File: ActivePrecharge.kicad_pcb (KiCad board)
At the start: 2 copper layers, 93.5 x 61.5 mm, 64 parts, among them IC1 AMC1311BDWVR, IC2 AMC1311BDWVR, IC3 1769205241, J1 Conn_01x02, J2 Conn_01x03, J3 Conn_01x02, Q1 IRLML0030, Q2 PMV35EPER, U3 AP63203WU, U4 Nucleo_L432KC

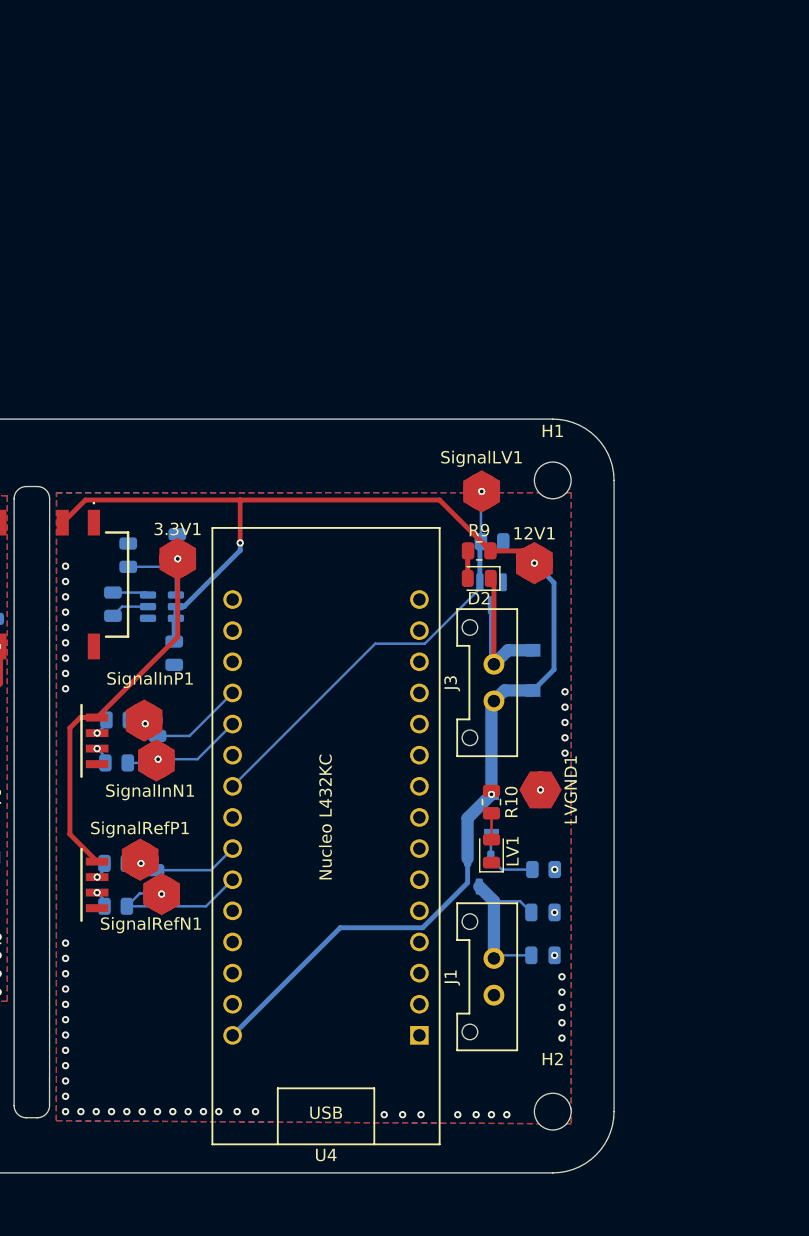
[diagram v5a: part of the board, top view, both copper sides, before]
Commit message: added contactor signal connectors from v.3
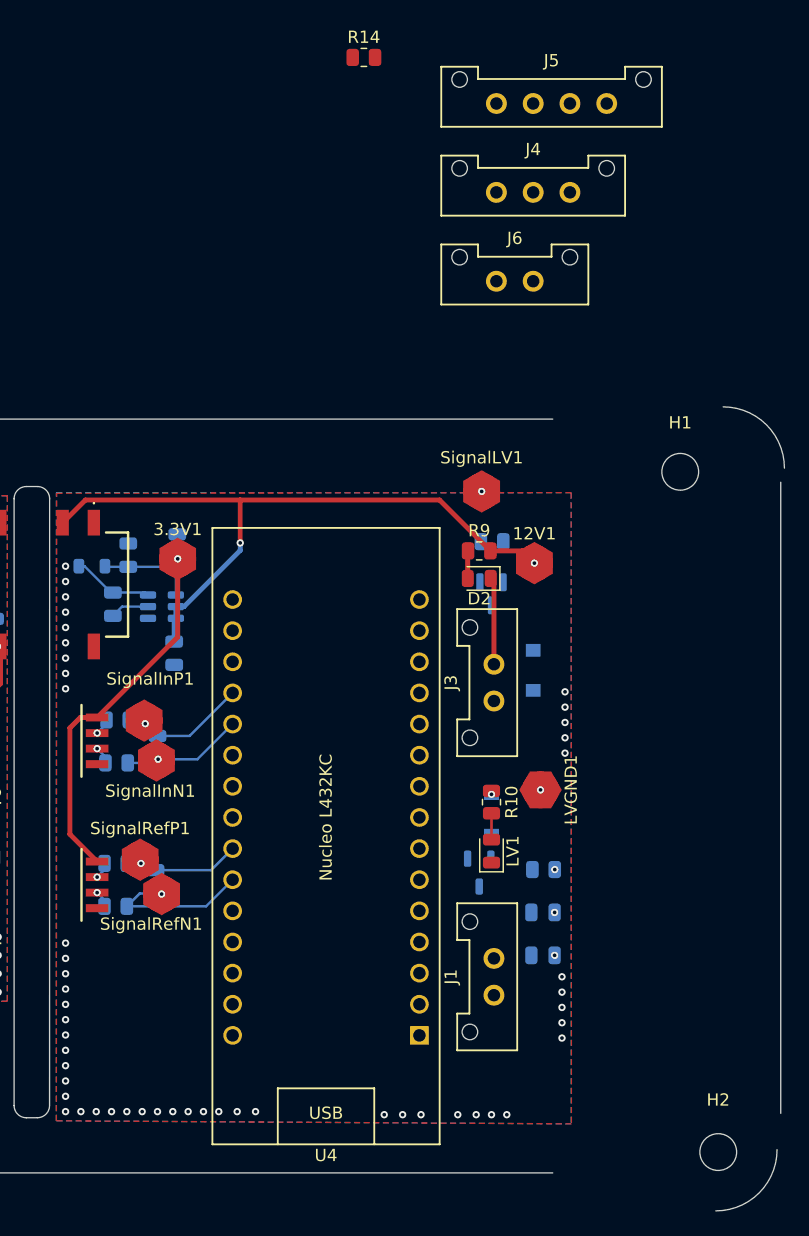
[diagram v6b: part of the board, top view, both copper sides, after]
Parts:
- added J4: Conn_01x03, utsvt-conn:Molex_MicroFit3.0_1x3xP3.00mm_PolarizingPeg_Vertical, F.Cu at (157.9, 41.0)
- added J5: Conn_01x04, utsvt-conn:Molex_MicroFit3.0_1x4xP3.00mm_PolarizingPeg_Vertical, F.Cu at (157.9, 33.8)
- added J6: Conn_01x02, utsvt-conn:Molex_MicroFit3.0_1x2xP3.00mm_PolarizingPeg_Vertical, F.Cu at (157.9, 48.2)
- added L1: 10u, Inductor_SMD:L_0805_2012Metric, B.Cu at (124.9, 71.5)
- added R14: R_US, Resistor_SMD:R_0805_2012Metric, F.Cu at (147.1, 30.0)
- moved H2 13.9 mm to (176.0, 119.3)
- moved H1 10.4 mm to (172.9, 63.8)
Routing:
- net /LV+: track 111.1 -> 55.5 mm
- net /SignalLV: track 34.8 -> 0.00 mm
- net +12V: track 12.9 -> 0.00 mm
- net Net-(D1-A): track 15.7 -> 7.11 mm
- net Net-(D7-A): track 5.75 -> 0.00 mm
- net Net-(U3-BST): track 2.95 -> 6.61 mm
- net /3.3V: track 37.4 -> 39.3 mm
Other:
- board size 93.5 x 61.5 mm -> 107.4 x 65.6 mm

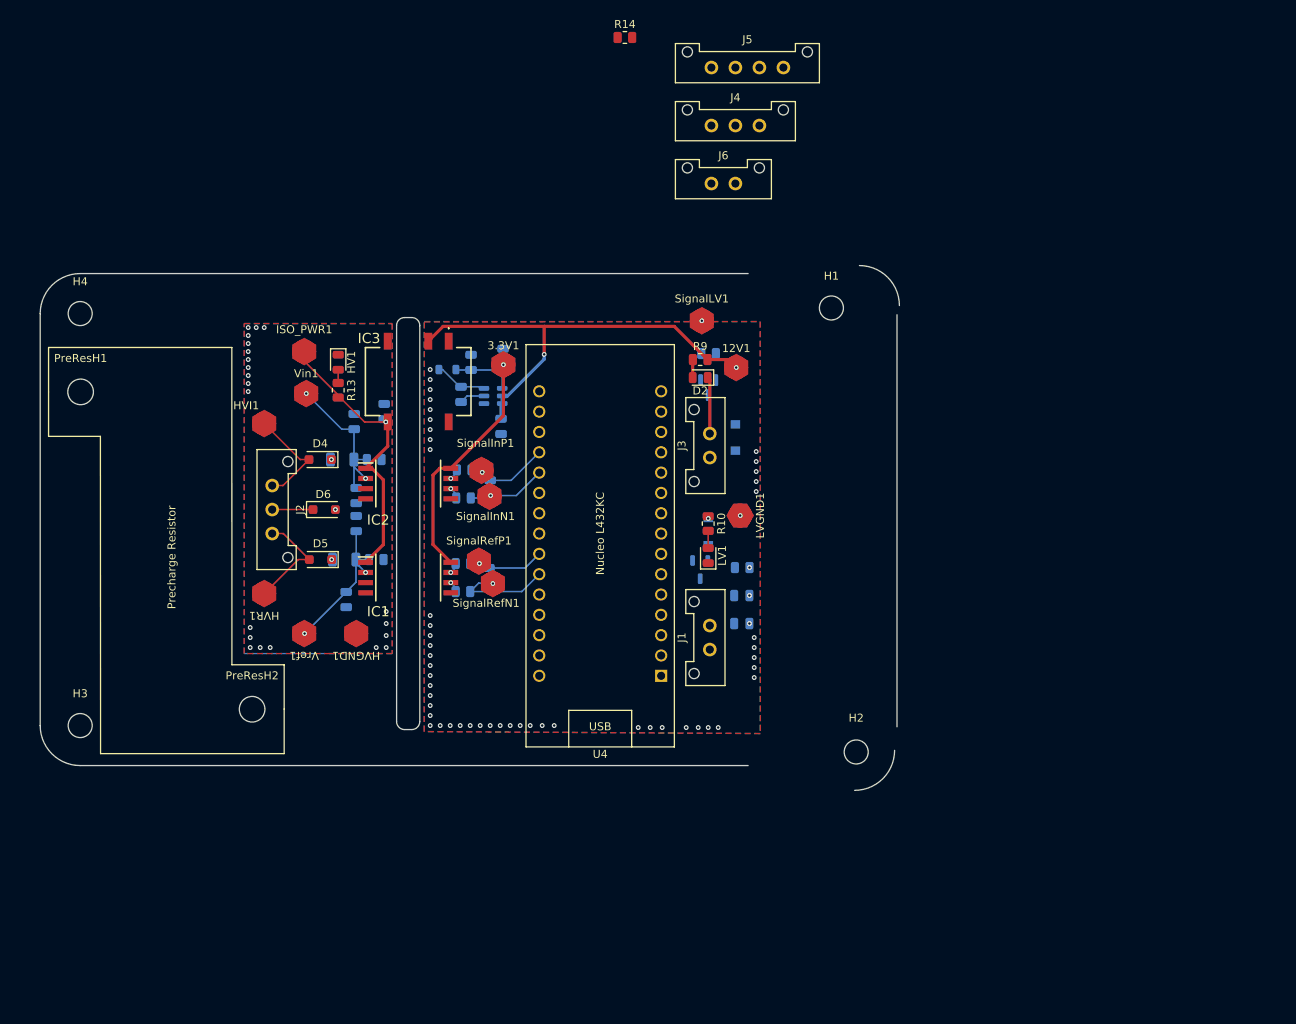
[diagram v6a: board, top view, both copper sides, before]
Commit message: verify controls signals and reverse polarity schematics
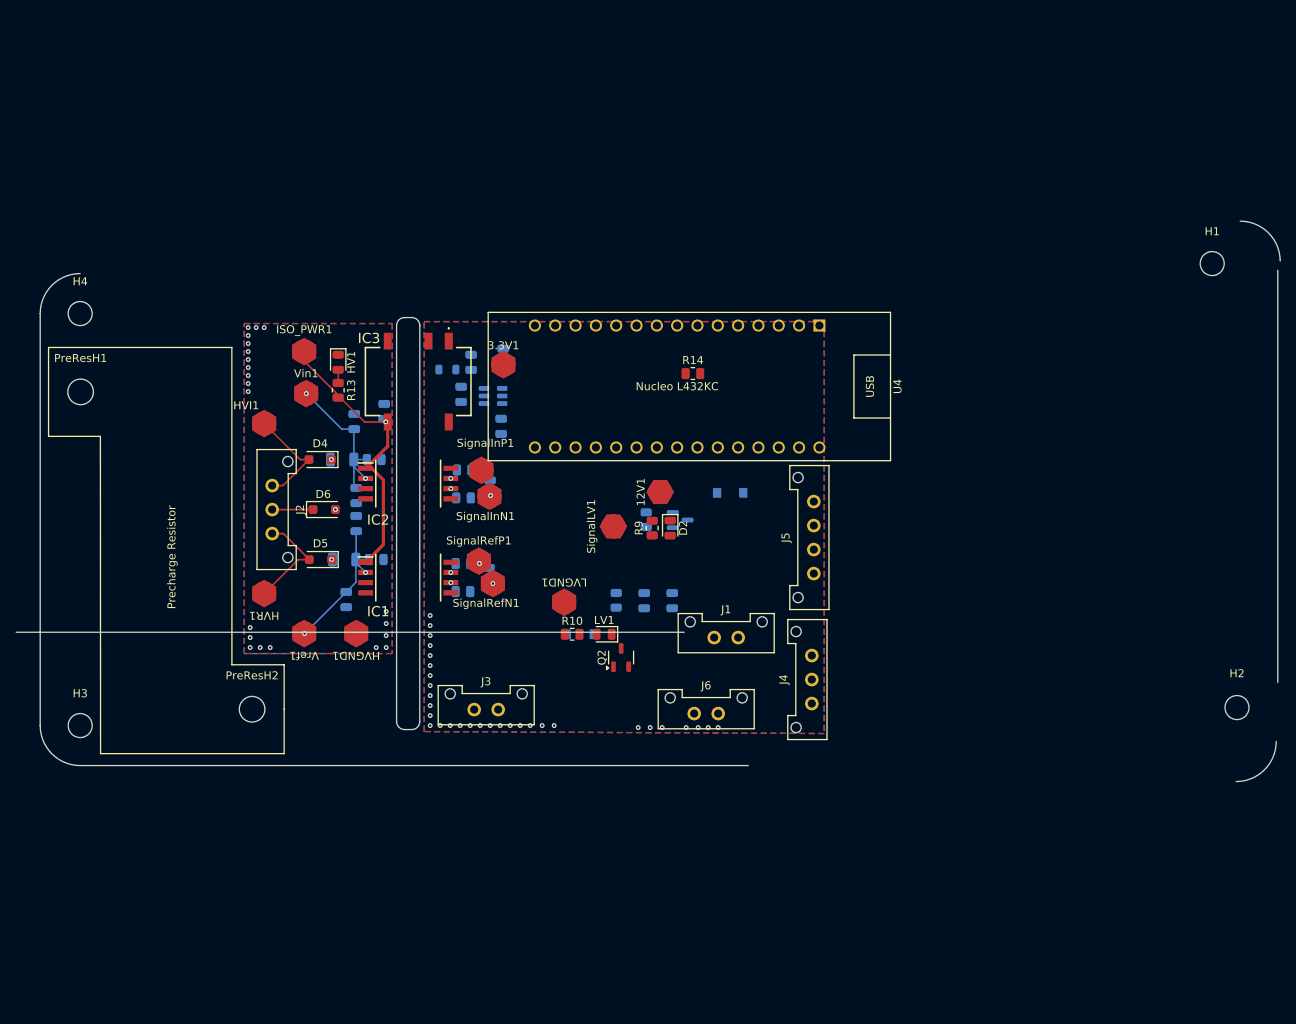
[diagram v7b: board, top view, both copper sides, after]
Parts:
- Q2: moved to F.Cu
- moved J4 73.3 mm to (170.4, 113.2), turned to 90 degrees
- moved J6 66.3 mm to (155.8, 114.5)
- moved J5 64.5 mm to (170.7, 97.0), turned to 90 degrees
- moved H1 47.9 mm to (220.5, 58.2)
- moved H2 47.9 mm to (223.6, 113.8)
- moved J3 43.1 mm to (128.2, 114.0), turned to 0 degrees
- moved R14 42.9 mm to (155.6, 72.0)
- moved SignalLV1 28.0 mm to (145.7, 91.1), turned to 90 degrees
- moved LVGND1 24.5 mm to (139.5, 100.6), turned to 180 degrees
- moved R11 22.2 mm to (149.8, 90.3), turned to 90 degrees
- moved R10 21.9 mm to (140.5, 104.6), turned to 0 degrees
- moved R9 21.9 mm to (150.5, 91.3), turned to 90 degrees
- moved U4 20.7 mm to (153.6, 73.6), turned to 180 degrees
- moved D7 20.5 mm to (141.5, 104.6), turned to 0 degrees
- moved D2 19.2 mm to (152.8, 91.3), turned to -90 degrees
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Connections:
- Q2 pad 1: /LV+ -> Net-(D7-A)
- Q2 pad 2: Net-(D7-A) -> /LV+
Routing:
- net /LV+: track 55.5 -> 0.00 mm, vias 3 -> 0
- net /3.3V: track 39.3 -> 0.00 mm, vias 1 -> 0
- net /SignalRefN: track 12.3 -> 0.00 mm
- net /SignalInP: track 10.5 -> 0.00 mm, vias 1 -> 0
- net /SignalInN: track 9.87 -> 0.00 mm
- net /SignalRefP: track 9.59 -> 0.00 mm
- net Net-(D1-A): track 7.11 -> 0.00 mm
- net Net-(U3-BST): track 6.61 -> 0.00 mm
- net Net-(U3-SW): track 3.17 -> 0.00 mm
- net Net-(D2-A): track 2.26 -> 0.00 mm
- net Net-(LV1-A): track 2.15 -> 0.00 mm
- net Net-(IC2-VOUTN): track 1.44 -> 0.00 mm
- net Net-(IC2-VOUTP): track 1.38 -> 0.00 mm
- net Net-(IC1-VOUTP): track 1.36 -> 0.00 mm
- net Net-(IC1-VOUTN): track 1.36 -> 0.00 mm
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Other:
- board size 107.4 x 65.6 mm -> 158 x 70 mm

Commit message: layout update with controls signals and fuses
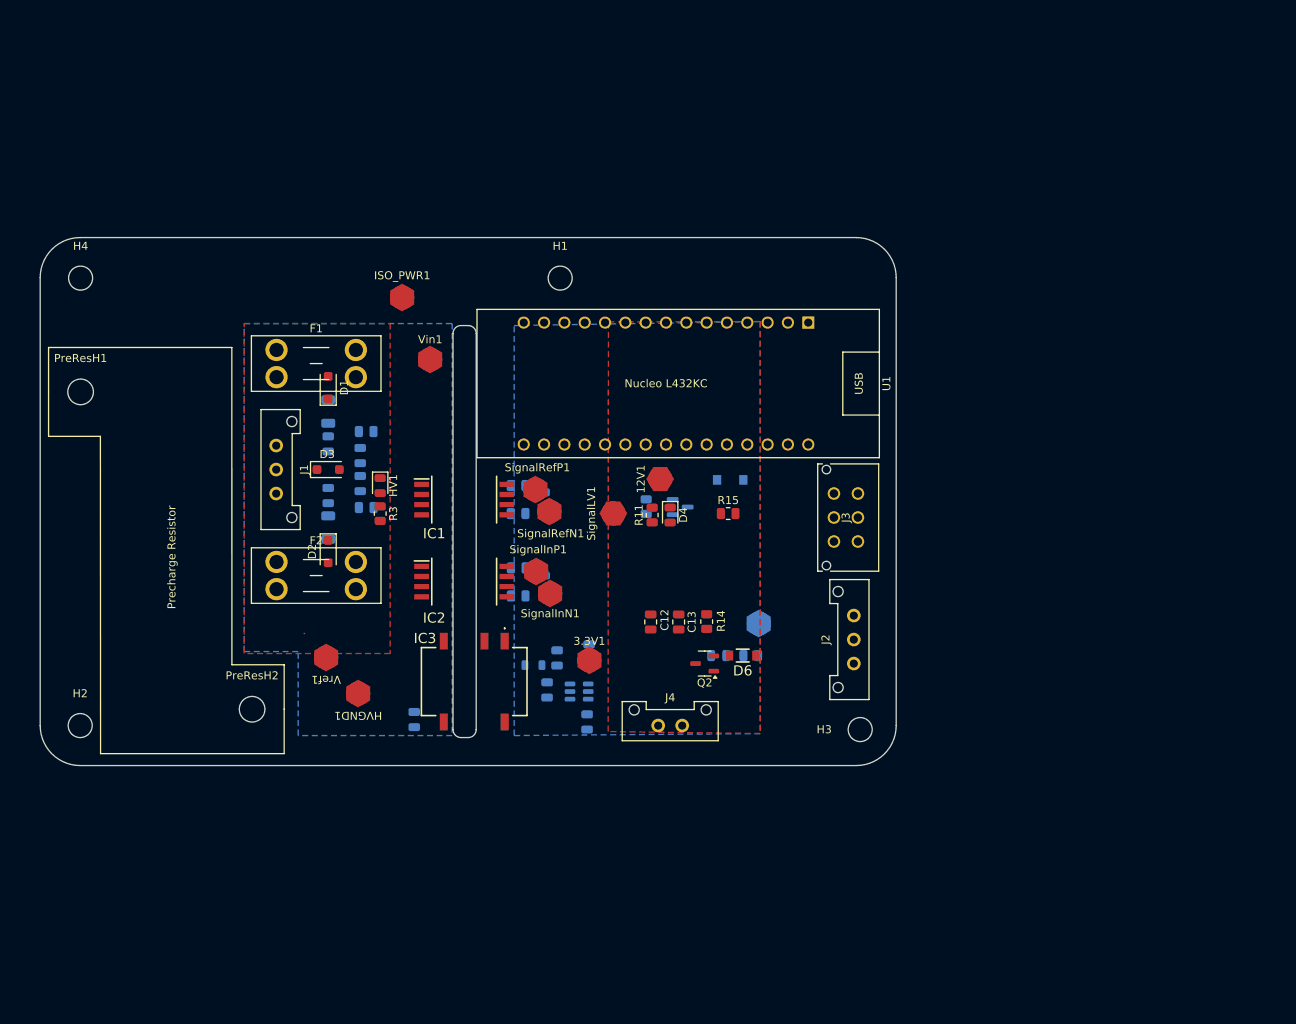
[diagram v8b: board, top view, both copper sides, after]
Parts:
- removed HVI1, HVR1: TestPoint, Active-PrechargeLib:TestPoint_HEX_3mmID
- removed the J4 at (170.4, 113.2)
- removed J5: Conn_01x04, utsvt-conn:Molex_MicroFit3.0_1x4xP3.00mm_PolarizingPeg_Vertical
- removed J6: Conn_01x02, utsvt-conn:Molex_MicroFit3.0_1x2xP3.00mm_PolarizingPeg_Vertical
- removed the R14 at (155.6, 72.0)
- added F1: Fuse, Fuse:Fuseholder_Blade_Mini_Keystone_3568, F.Cu at (103.5, 69.0)
- added F2: Fuse, Fuse:Fuseholder_Blade_Mini_Keystone_3568, F.Cu at (103.5, 95.5)
- added J2: Conn_01x03, utsvt-conn:Molex_MicroFit3.0_1x3xP3.00mm_PolarizingPeg_Vertical, F.Cu at (175.7, 108.2)
- added R15: 10k, Resistor_SMD:R_0805_2012Metric, F.Cu at (160.0, 89.5)
- C12: renamed from C1; moved to F.Cu
- C13: renamed from C2; moved to F.Cu
- D6: renamed from D7; moved to F.Cu
- J3: value Conn_01x02 -> Conn_02x03_Top_Bottom; footprint utsvt-conn:Molex_MicroFit3.0_1x2xP3.00mm_PolarizingPeg_Vertical -> Active-PrechargeLib:CONN_SD-43045-005_06_MOL
- LV1, LVGND1: moved to B.Cu
- R13: renamed from R10; moved to B.Cu
- R14: renamed from R12; moved to F.Cu
- moved H1 81.5 mm to (139.0, 60.1)
- moved J3 55.0 mm to (176.2, 87.0), turned to 90 degrees
- moved H3 47.2 mm to (176.5, 116.5)
- moved C2 38.7 mm to (120.8, 115.2)
- moved C10 38.5 mm to (137.4, 111.5)
- moved C11 38.5 mm to (142.4, 115.5)
- moved C8 38.5 mm to (142.6, 106.8)
- moved C9 38.5 mm to (138.6, 107.5)
- moved L1 38.5 mm to (135.7, 108.5)
- moved U2 38.5 mm to (141.4, 111.8)
- moved 3.3V1 38.5 mm to (142.7, 107.8)
- moved IC3 38.1 mm to (128.2, 110.5)
- moved LVGND1 24.5 mm to (163.8, 103.2), turned to 0 degrees
- moved R13 22.5 mm to (162.8, 107.2), turned to 180 degrees
- moved D6 20.5 mm to (161.8, 107.2), turned to 180 degrees
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- renumbered C7 to C1, C4 to C10, C6 to C11, C10 to C2, C15 to C3, C9 to C4, C3 to C5, C12 to C6, C8 to C7, C13 to C8, C5 to C9, D4 to D1, D5 to D2, D6 to D3, D2 to D4, D1 to D5, H3 to H2, H2 to H3, J2 to J1, J1 to J4, R11 to R10, R9 to R11, R13 to R3, R3 to R4, R4 to R5, R7 to R6, R8 to R7, R5 to R8, R6 to R9, U4 to U1, U3 to U2
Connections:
- 12V1 pad 1: /LV+ -> /Con+
- C11 pad 2: /LV+ -> /Con+
- D1 pad 2: /HIn -> Net-(D1-A)
- D2 pad 2: HRef -> Net-(D2-A)
- D4 pad 1: Net-(D1-A) -> /Con-
- D5 pad 1: /LV+ -> /Con+
- D5 pad 2: Net-(D1-A) -> /Con-
- D6 pad 1: /LV+ -> /Con+
- IC3 pad 2: /LV+ -> /Con+
- J3 pad 1: /LV+ -> /Con+
- J3 pad 2: Net-(D1-A) -> /Con+
- Q1 pad 3: Net-(D1-A) -> /Con-
- Q2 pad 2: /LV+ -> /Con+
- R11 pad 2: /LV+ -> /Con+
- R13 pad 1: /LV+ -> /Con+
- U1 pad 30: /LV+ -> /Con+
- U2 pad 2: /LV+ -> /Con+
- U2 pad 3: /LV+ -> /Con+
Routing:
- net /ISO_PWR: track 36.0 -> 0.00 mm, vias 1 -> 0
- net /Vin: track 19.9 -> 0.00 mm, vias 2 -> 0
- net /Vref: track 19.3 -> 0.05 mm, vias 2 -> 0
- net /HIn: track 13.4 -> 0.00 mm
- net HRef: track 13.4 -> 0.00 mm
- net HGND: track 5.10 -> 0.00 mm
- net Net-(HV1-A): track 1.65 -> 0.00 mm
- net Net-(IC2-VOUTP): vias 1 -> 0
- net Net-(IC2-VOUTN): vias 1 -> 0
- net Net-(IC1-VOUTP): vias 1 -> 0
- net Net-(IC1-VOUTN): vias 1 -> 0
- net LVGND: vias 31 -> 0
- net /SignalRefP: vias 1 -> 0
- net /SignalRefN: vias 1 -> 0
- net /SignalInN: vias 1 -> 0
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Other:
- board size 158 x 70 mm -> 107 x 66 mm
